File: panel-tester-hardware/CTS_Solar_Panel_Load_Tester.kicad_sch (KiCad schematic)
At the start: 10 parts, among them J1 Screw_Terminal_01x02, J2 Conn_01x02_Pin, U1 INA219AxD, U2 YAAJ_BluePill

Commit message: Add files via upload
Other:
- note added: "I2C Address 0x40"
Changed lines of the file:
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@@
+		)
+	)
+	(text "I2C Address 0x40"
+		(exclude_from_sim no)
+		(at 203.454 49.022 0)
+		(effects
+			(font
+				(size 1.27 1.27)
+			)
 		)
 	)

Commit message: Fix potentiometer schematic and import custom footprint
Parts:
- RV1: footprint (none) -> Potentiometer_Custom:3310C101102L
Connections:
- net GND: now also RV1.2; no longer RV1.3
- net MCU_ADC_SENSE: no longer RV1.2
- no-connect marks 0 -> 1
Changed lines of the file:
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@@
 		(color 0 0 0 0)
 	)
+	(no_connect
+		(at 151.13 60.96)
+	)
 	(wire
 		(pts
@@
 	(wire
 		(pts
+			(xy 156.21 57.15) (xy 154.94 57.15)
+		)
+		(stroke
+			(width 0)
+			(type default)
+		)
+	)
+	(wire
+		(pts
 			(xy 151.13 52.07) (xy 151.13 53.34)
 		)
@@
 	(wire
 		(pts
+			(xy 156.21 57.15) (xy 156.21 58.42)
+		)
+		(stroke
+			(width 0)
+			(type default)
+		)
+	)
+	(wire
+		(pts
 			(xy 74.93 40.64) (xy 76.2 40.64)
 		)
@@
 	(wire
 		(pts
-			(xy 154.94 62.23) (xy 154.94 57.15)
-		)
-		(stroke
-			(width 0)
-			(type default)
-		)
-	)
-	(wire
-		(pts
 			(xy 76.2 39.37) (xy 76.2 40.64)
-		)
-		(stroke
-			(width 0)
-			(type default)
-		)
-	)
-	(wire
-		(pts
-			(xy 151.13 62.23) (xy 151.13 60.96)
 		)
 		(stroke
@@
 	(global_label "MCU_ADC_SENSE"
 		(shape input)
-		(at 154.94 62.23 0)
+		(at 162.56 66.04 0)
 		(fields_autoplaced yes)
 		(effects
@@
 		)
 		(property "Intersheetrefs" "${INTERSHEET_REFS}"
-			(at 173.5884 62.23 0)
+			(at 181.2084 66.04 0)
 			(effects
 				(font
@@
 	)
 	(symbol
-		(lib_id "power:GND")
-		(at 151.13 62.23 0)
-		(unit 1)
-		(exclude_from_sim no)
-		(in_bom yes)
-		(on_board yes)
-		(dnp no)
-		(fields_autoplaced yes)
-		(property "Reference" "#PWR04"
-			(at 151.13 68.58 0)
-			(effects
-				(font
-					(size 1.27 1.27)
-				)
-				(hide yes)
-			)
-		)
-		(property "Value" "GND"
-			(at 151.13 67.31 0)
-			(effects
-				(font
-					(size 1.27 1.27)
-				)
-			)
-		)
-		(property "Footprint" ""
-			(at 151.13 62.23 0)
-			(effects
-				(font
-					(size 1.27 1.27)
-				)
-				(hide yes)
-			)
-		)
-		(property "Datasheet" ""
-			(at 151.13 62.23 0)
-			(effects
-				(font
-					(size 1.27 1.27)
-				)
-				(hide yes)
-			)
-		)
-		(property "Description" "Power symbol creates a global label with name \"GND\" , ground"
-			(at 151.13 62.23 0)
-			(effects
-				(font
-					(size 1.27 1.27)
-				)
-				(hide yes)
-			)
-		)
-		(pin "1"
-		)
-		(instances
-			(project ""
-				(path "/211b8366-2b1c-422c-86f1-173703c1ab0a"
-					(reference "#PWR04")
-					(unit 1)
-				)
-			)
-		)
-	)
-	(symbol
 		(lib_id "Device:R")
 		(at 35.56 82.55 0)
@@
 			)
 		)
-		(property "Footprint" ""
+		(property "Footprint" "Potentiometer_Custom:3310C101102L"
 			(at 151.13 57.15 0)
 			(effects
@@
 		(exclude_from_sim no)
 		(in_bom yes)
-		(on_board yes)
+		(on_board no)
 		(dnp no)
 		(fields_autoplaced yes)
@@
 					(unit 1)
 				)
+			)
+		)
+	)
+	(symbol
+		(lib_id "power:GND")
+		(at 156.21 58.42 0)
+		(unit 1)
+		(exclude_from_sim no)
+		(in_bom yes)
+		(on_board yes)
+		(dnp no)
+		(fields_autoplaced yes)
+		(property "Reference" "#PWR012"
+			(at 156.21 64.77 0)
+			(effects
+				(font
+					(size 1.27 1.27)
+				)
+				(hide yes)
+			)
+		)
+		(property "Value" "GND"
+			(at 156.21 63.5 0)
+			(effects
+				(font
+					(size 1.27 1.27)
+				)
+			)
+		)
+		(property "Footprint" ""
+			(at 156.21 58.42 0)
+			(effects
+				(font
+					(size 1.27 1.27)
+				)
+				(hide yes)
+			)
+		)
+		(property "Datasheet" ""
+			(at 156.21 58.42 0)
+			(effects
+				(font
+					(size 1.27 1.27)
+				)
+				(hide yes)
+			)
+		)
+		(property "Description" "Power symbol creates a global label with name \"GND\" , ground"
+			(at 156.21 58.42 0)
+			(effects
+				(font
+					(size 1.27 1.27)
+				)
+				(hide yes)
+			)
+		)
+		(pin "1"
+		)
+		(instances
+			(project "CTS_Solar_Panel_Load_Tester"
+				(path "/211b8366-2b1c-422c-86f1-173703c1ab0a"
+					(reference "#PWR012")
+					(unit 1)
+				)

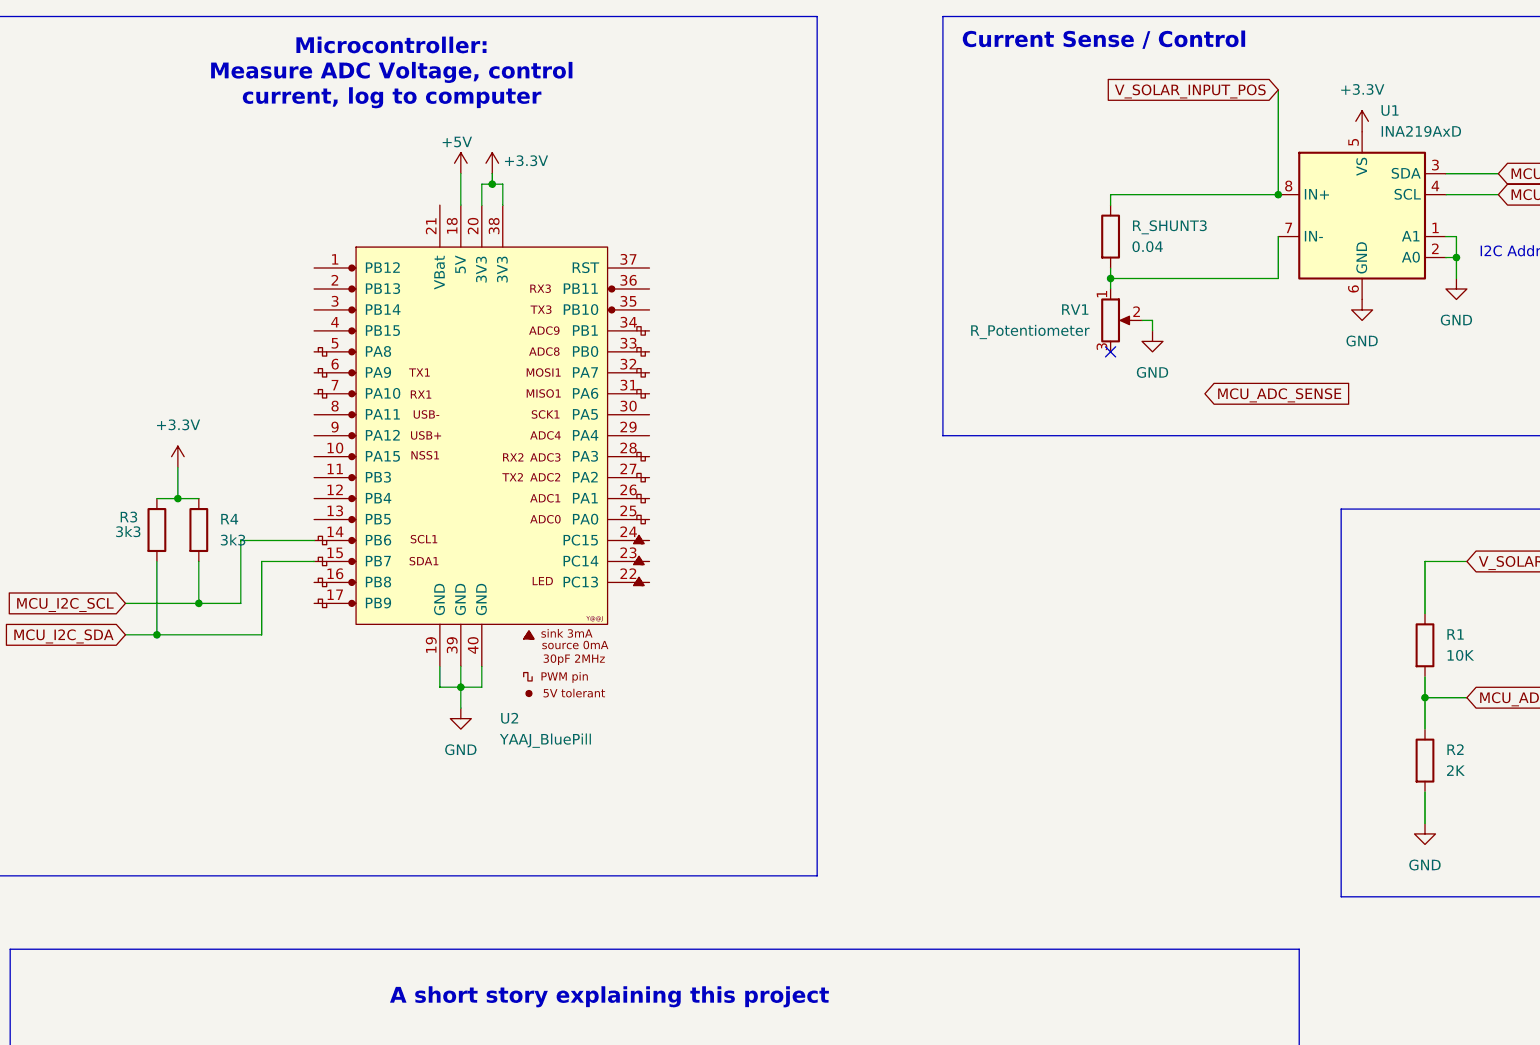
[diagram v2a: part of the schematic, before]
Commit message: Add microcontroller breakout pins, update potentiometer footprint
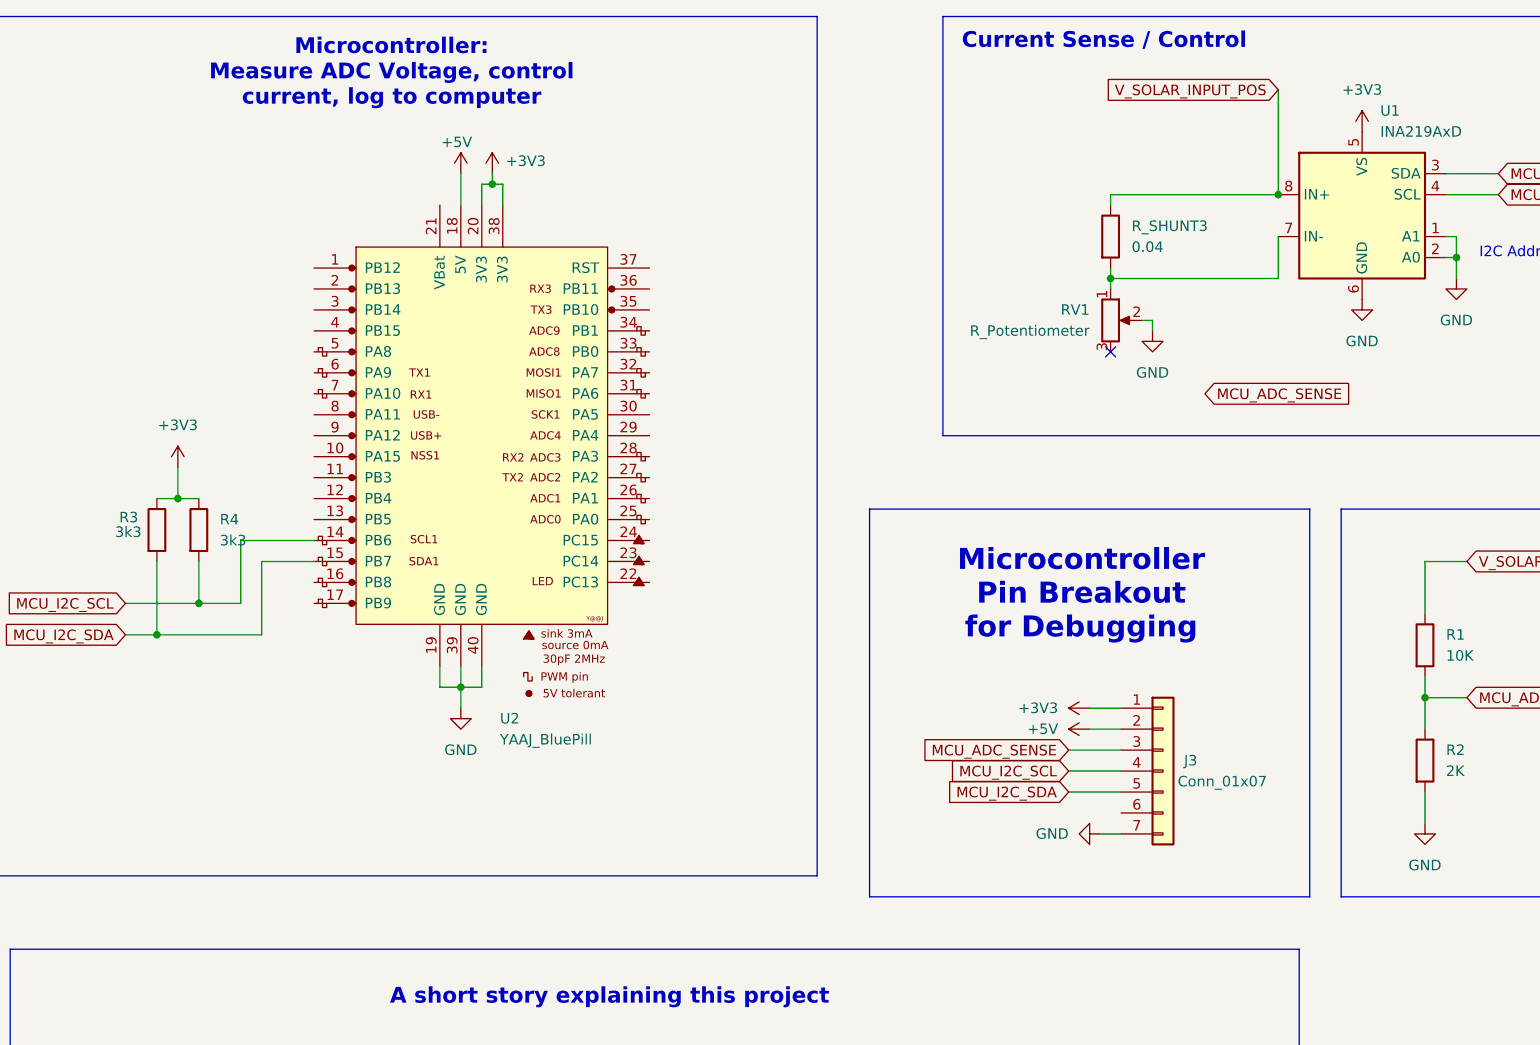
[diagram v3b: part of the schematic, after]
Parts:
- added J3: Conn_01x07, Connector_PinHeader_2.54mm:PinHeader_1x07_P2.54mm_Vertical, symbol Connector_Generic:Conn_01x07
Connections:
- net +5V: now also J3.2 (Pin_2)
- net GND: now also J3.7 (Pin_7)
- net MCU_ADC_SENSE: now also J3.3 (Pin_3)
- net MCU_I2C_SCL: now also J3.4 (Pin_4)
- net MCU_I2C_SDA: now also J3.5 (Pin_5)
- net +3.3V renamed +3V3
- net +3V3: now also J3.1 (Pin_1)
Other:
- note added: "Microcontroller Pin Breakout for Debugging"

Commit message: Bluepill layout edits
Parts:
- U2: footprint (none) -> BluePill:YAAJ_BluePill_2
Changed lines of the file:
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@@
 			)
 		)
-		(property "Footprint" ""
+		(property "Footprint" "BluePill:YAAJ_BluePill_2"
 			(at 73.025 46.99 90)
 			(effects

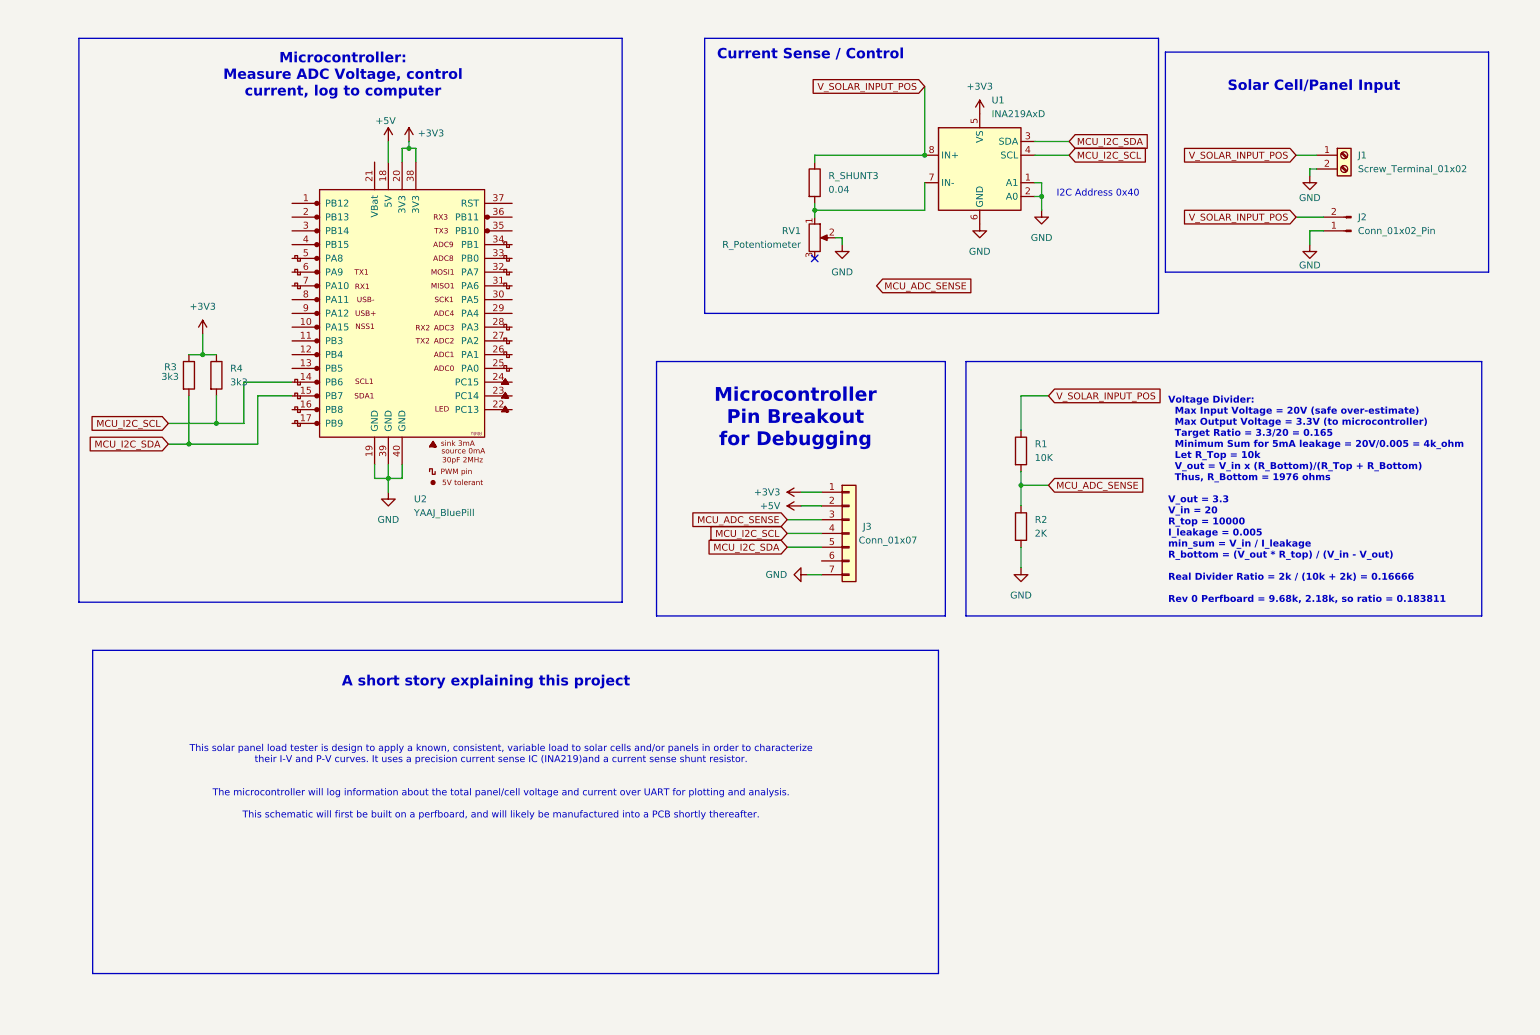
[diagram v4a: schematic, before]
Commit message: ERC/DRC fixes
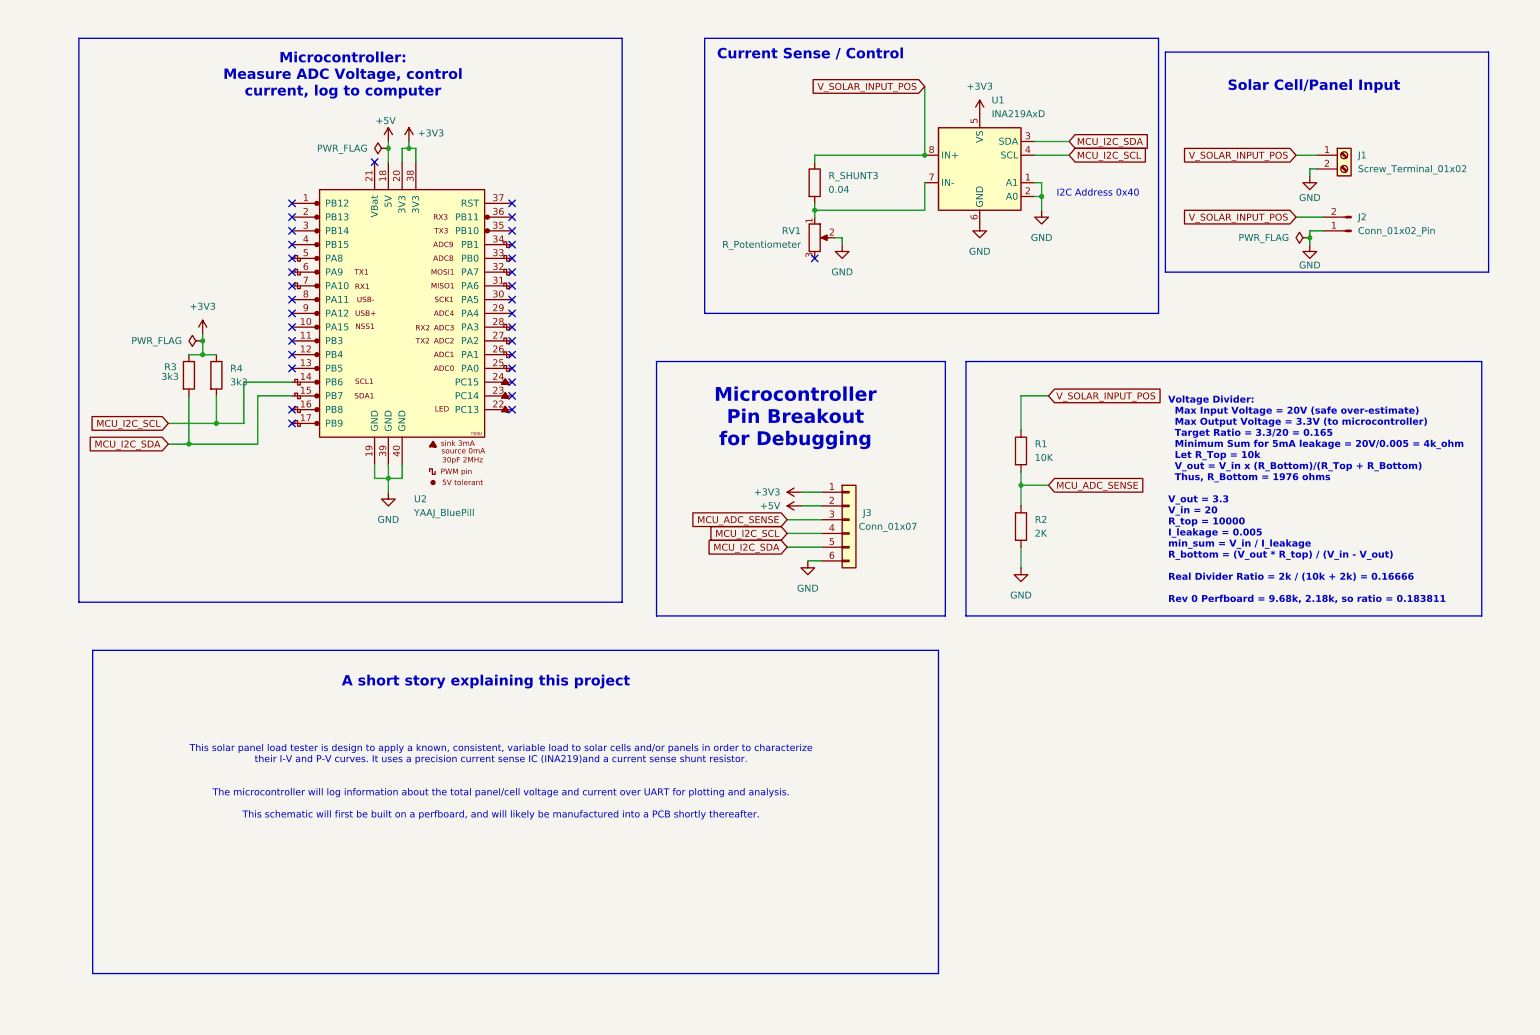
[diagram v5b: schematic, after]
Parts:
- J3: footprint Connector_PinHeader_2.54mm:PinHeader_1x07_P2.54mm_Vertical -> Connector_PinHeader_2.54mm:PinHeader_1x06_P2.54mm_Vertical; symbol Connector_Generic:Conn_01x07 -> Connector_Generic:Conn_01x06
- RV1: footprint Potentiometer_Custom:3310C101102L -> PotentiometerCustom:3310C101102L
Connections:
- net GND: now also J3.6 (Pin_6); no longer J3.7 (Pin_7)
- no-connect marks 1 -> 33

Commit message: Schematic fixes + UART breakout header
TODO: Confirm R_shunt value
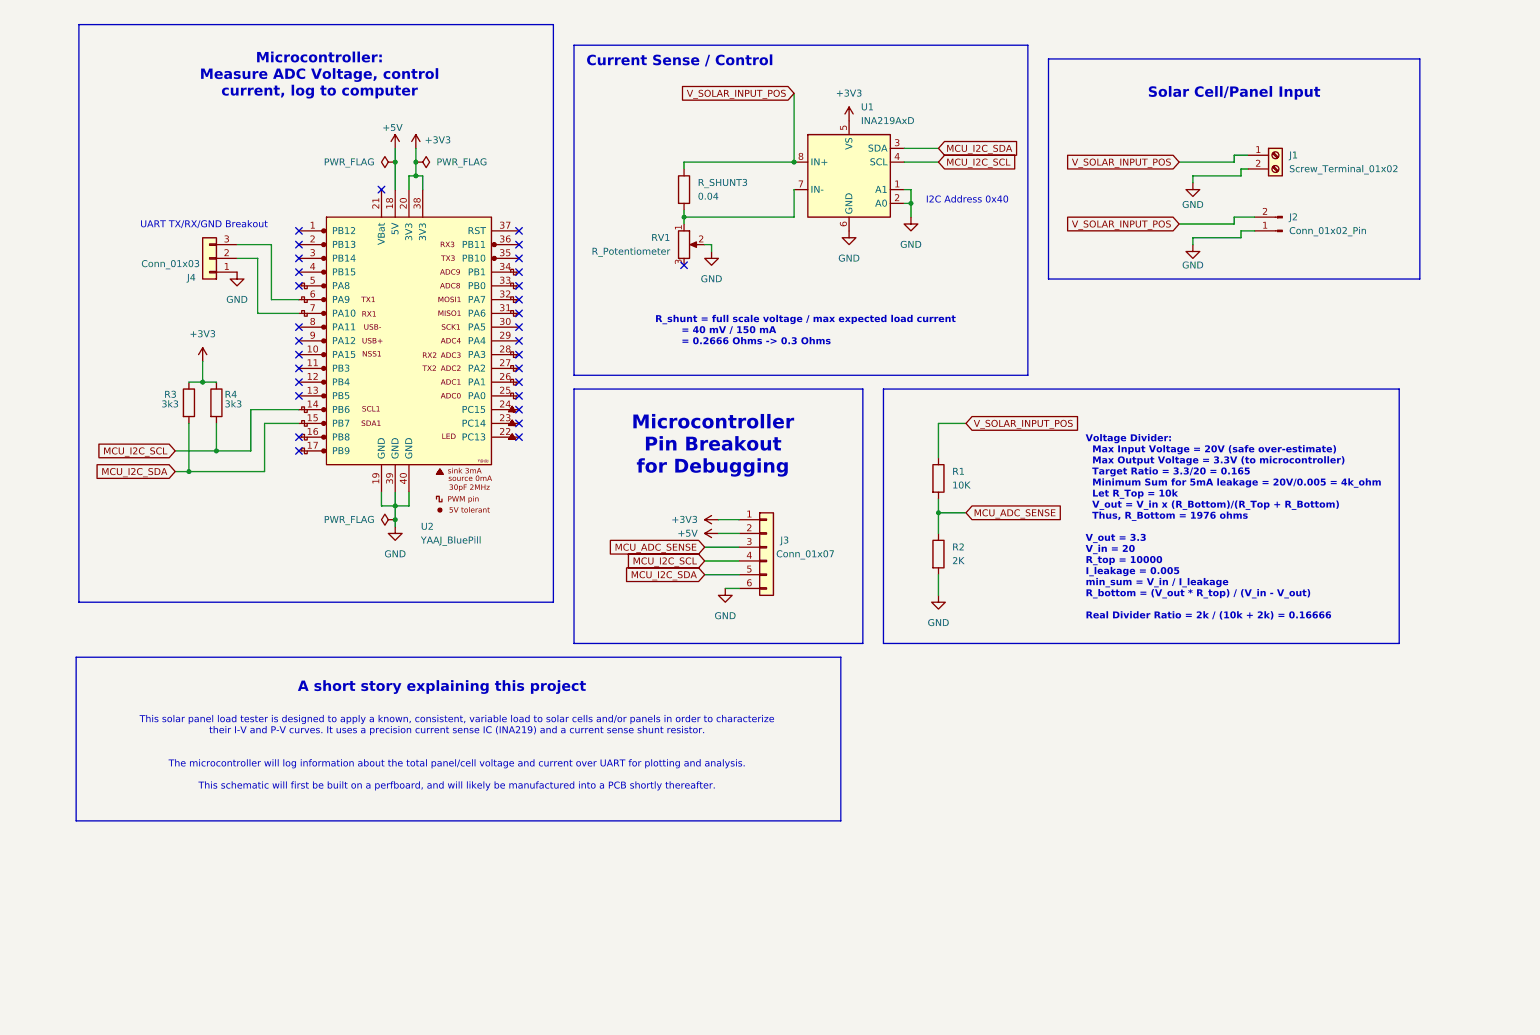
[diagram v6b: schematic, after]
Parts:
- added J4: Conn_01x03, Connector_PinHeader_2.54mm:PinHeader_1x03_P2.54mm_Vertical, symbol Connector_Generic:Conn_01x03
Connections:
- net GND: now also J4.1 (Pin_1)
- net at U2.6 (PA9): now also J4.3 (Pin_3)
- net at U2.7 (PA10): now also J4.2 (Pin_2)
- no-connect marks 33 -> 31
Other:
- note added: "R_shunt = full scale voltage / max expected load current = 40 mV / 150 mA = 0.2666 Ohms -> 0.3 Ohms"
- note added: "This solar panel load tester is designed to apply a known, consistent, variable load to solar cells and/or panels in order to characterize their I-V and P-V curves. It uses a precision current sense IC (INA219) and a current sense shunt resistor. The microcontroller will log information about the total panel/cell voltage and current over UART for plotting and analysis. This schematic will first b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"
- note added: "UART TX/RX/GND Breakout"
- note removed: "This solar panel load tester is design to apply a known, consistent, variable load to solar cells and/or panels in order to characterize their I-V and P-V curves. It uses a precision current sense IC (INA219)and a current sense shunt resistor. The microcontroller will log information about the total panel/cell voltage and current over UART for plotting and analysis. This schematic will first be b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"
- moved on the sheet: J1, J2, J3, R1, R2, R3, R4, RV1, R_SHUNT3, U1, U2
